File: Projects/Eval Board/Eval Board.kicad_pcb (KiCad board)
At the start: 4 copper layers, 46 x 27.3 mm, 37 parts, among them J1 LO, J2 Q OUT, J3 I Out, J4 Q OUT, J6 Conn_01x02, J7 Conn_01x04, J8 Conn_01x05, U1 LTC5584

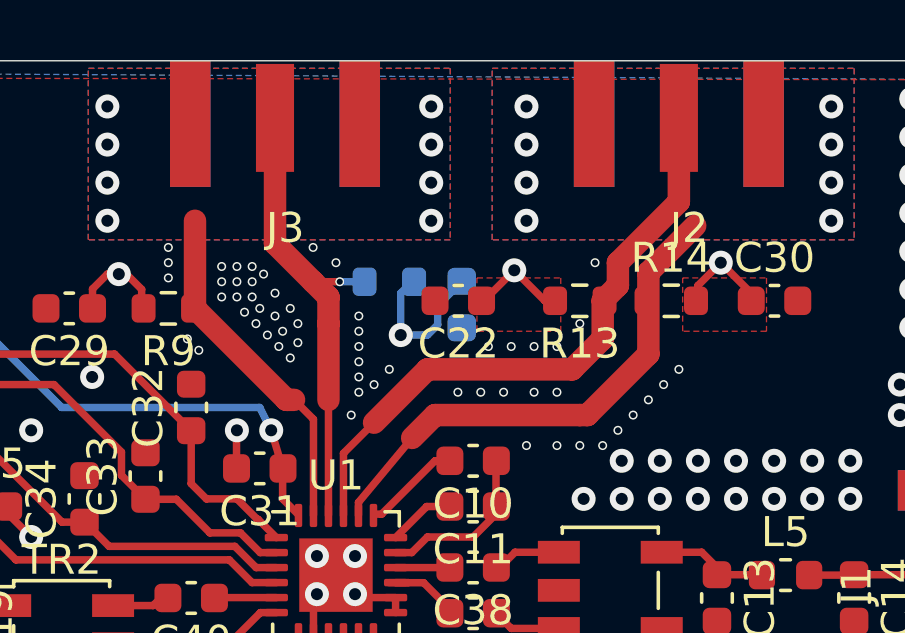
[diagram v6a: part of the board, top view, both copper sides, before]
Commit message: Widened the traces on the I+-/Q+- to be 1mm
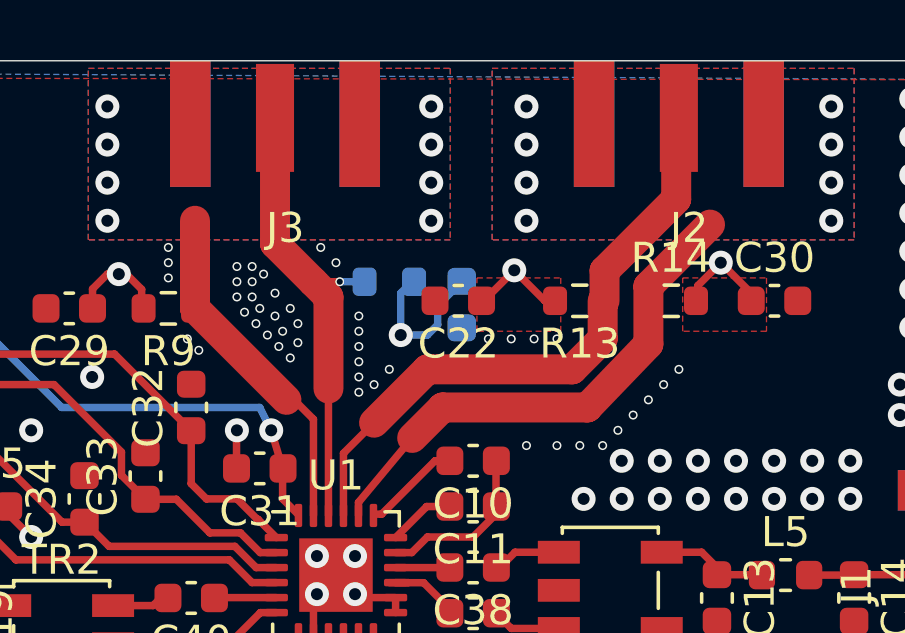
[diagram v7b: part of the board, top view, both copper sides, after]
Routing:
- net /Q+: track 21.0 -> 26.9 mm
- net GND: vias 199 -> 188
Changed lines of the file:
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@@
     (thickness 1.6)
     (drawings 8)
-    (tracks 407)
+    (tracks 396)
     (zones 0)
     (modules 37)
@@
   )
   (setup
-    (last_trace_width 0.75)
+    (last_trace_width 1)
     (user_trace_width 0.5)
     (user_trace_width 0.75)
@@
   (segment (start 194.83 83.554) (end 195.072 83.312) (width 0.25) (layer F.Cu) (net 4) (status 30))
   (segment (start 194.83 84.5375) (end 194.83 83.554) (width 0.25) (layer F.Cu) (net 4) (status 30))
-  (via (at 191.77 73.279) (size 0.3) (drill 0.2) (layers F.Cu B.Cu) (net 4))
-  (via (at 191.77 72.771) (size 0.3) (drill 0.2) (layers F.Cu B.Cu) (net 4))
-  (via (at 191.77 72.263) (size 0.3) (drill 0.2) (layers F.Cu B.Cu) (net 4))
   (via (at 192.278 72.263) (size 0.3) (drill 0.2) (layers F.Cu B.Cu) (net 4))
   (via (at 192.786 72.263) (size 0.3) (drill 0.2) (layers F.Cu B.Cu) (net 4))
@@
   (via (at 189.992 72.136) (size 0.3) (drill 0.2) (layers F.Cu B.Cu) (net 4))
   (via (at 189.992 71.628) (size 0.3) (drill 0.2) (layers F.Cu B.Cu) (net 4))
-  (via (at 199.644 76.454) (size 0.3) (drill 0.2) (layers F.Cu B.Cu) (net 4))
-  (via (at 200.406 76.454) (size 0.3) (drill 0.2) (layers F.Cu B.Cu) (net 4))
-  (via (at 201.168 76.454) (size 0.3) (drill 0.2) (layers F.Cu B.Cu) (net 4))
-  (via (at 202.184 76.454) (size 0.3) (drill 0.2) (layers F.Cu B.Cu) (net 4))
-  (via (at 202.946 76.454) (size 0.3) (drill 0.2) (layers F.Cu B.Cu) (net 4))
   (via (at 207.01 75.692) (size 0.3) (drill 0.2) (layers F.Cu B.Cu) (net 4))
   (via (at 206.502 76.2) (size 0.3) (drill 0.2) (layers F.Cu B.Cu) (net 4))
@@
   (via (at 202.946 78.232) (size 0.3) (drill 0.2) (layers F.Cu B.Cu) (net 4))
   (via (at 204.978 77.724) (size 0.3) (drill 0.2) (layers F.Cu B.Cu) (net 4))
-  (via (at 200.66 74.93) (size 0.3) (drill 0.2) (layers F.Cu B.Cu) (net 4))
-  (via (at 201.422 74.93) (size 0.3) (drill 0.2) (layers F.Cu B.Cu) (net 4))
-  (via (at 202.184 74.93) (size 0.3) (drill 0.2) (layers F.Cu B.Cu) (net 4))
-  (via (at 202.946 74.93) (size 0.3) (drill 0.2) (layers F.Cu B.Cu) (net 4))
-  (via (at 203.708 74.168) (size 0.3) (drill 0.2) (layers F.Cu B.Cu) (net 4))
-  (via (at 204.216 72.136) (size 0.3) (drill 0.2) (layers F.Cu B.Cu) (net 4))
+  (via (at 200.66 74.676) (size 0.3) (drill 0.2) (layers F.Cu B.Cu) (net 4))
+  (via (at 201.422 74.676) (size 0.3) (drill 0.2) (layers F.Cu B.Cu) (net 4))
+  (via (at 202.184 74.676) (size 0.3) (drill 0.2) (layers F.Cu B.Cu) (net 4))
+  (via (at 202.946 74.676) (size 0.3) (drill 0.2) (layers F.Cu B.Cu) (net 4))
   (via (at 196.85 76.2) (size 0.3) (drill 0.2) (layers F.Cu B.Cu) (net 4))
   (via (at 197.358 75.692) (size 0.3) (drill 0.2) (layers F.Cu B.Cu) (net 4))
-  (via (at 196.088 77.216) (size 0.3) (drill 0.2) (layers F.Cu B.Cu) (net 4))
   (via (at 193.802 74.422) (size 0.3) (drill 0.2) (layers F.Cu B.Cu) (net 4))
   (via (at 193.548 73.914) (size 0.3) (drill 0.2) (layers F.Cu B.Cu) (net 4))
   (via (at 195.58 72.136) (size 0.3) (drill 0.2) (layers F.Cu B.Cu) (net 4))
-  (via (at 194.818 71.628) (size 0.3) (drill 0.2) (layers F.Cu B.Cu) (net 4))
+  (via (at 195.072 71.628) (size 0.3) (drill 0.2) (layers F.Cu B.Cu) (net 4))
   (via (at 203.708 78.232) (size 0.3) (drill 0.2) (layers F.Cu B.Cu) (net 4))
   (via (at 204.47 78.232) (size 0.3) (drill 0.2) (layers F.Cu B.Cu) (net 4))
@@
   (segment (start 195.83 80.5625) (end 195.83 78.49) (width 0.25) (layer F.Cu) (net 18))
   (segment (start 195.83 78.49) (end 196.85 77.47) (width 0.25) (layer F.Cu) (net 18))
-  (segment (start 204.978 72.898) (end 204.978 72.136) (width 0.75) (layer F.Cu) (net 18))
   (segment (start 204.978 72.136) (end 207.01 70.104) (width 0.75) (layer F.Cu) (net 18))
   (segment (start 207.01 70.104) (end 207.01 67.056) (width 0.75) (layer F.Cu) (net 18))
-  (segment (start 196.85 77.47) (end 198.628 75.692) (width 0.75) (layer F.Cu) (net 18))
-  (segment (start 198.628 75.692) (end 203.454 75.692) (width 0.75) (layer F.Cu) (net 18))
-  (segment (start 203.454 75.692) (end 204.47 74.676) (width 0.75) (layer F.Cu) (net 18))
-  (segment (start 204.47 73.406) (end 204.978 72.898) (width 0.75) (layer F.Cu) (net 18))
-  (segment (start 204.47 74.676) (end 204.47 73.406) (width 0.75) (layer F.Cu) (net 18))
+  (segment (start 196.85 77.47) (end 198.628 75.692) (width 1) (layer F.Cu) (net 18))
+  (segment (start 198.628 75.692) (end 203.454 75.692) (width 1) (layer F.Cu) (net 18))
+  (segment (start 203.454 75.692) (end 204.47 74.676) (width 1) (layer F.Cu) (net 18))
+  (segment (start 204.47 74.676) (end 204.47 73.406) (width 1) (layer F.Cu) (net 18))
+  (segment (start 204.533 72.404224) (end 206.921612 70.015612) (width 1) (layer F.Cu) (net 18))
+  (segment (start 204.533 73.406) (end 204.533 72.404224) (width 1) (layer F.Cu) (net 18))
+  (segment (start 206.921612 70.015612) (end 206.921612 67.144388) (width 1) (layer F.Cu) (net 18))
+  (segment (start 206.921612 67.144388) (end 207.01 67.056) (width 1) (layer F.Cu) (net 18))
   (segment (start 195.33 80.5625) (end 195.33 76.712) (width 0.25) (layer F.Cu) (net 19))
-  (segment (start 193.548 71.501) (end 193.548 67.056) (width 0.75) (layer F.Cu) (net 19))
-  (segment (start 195.33 76.712) (end 195.33 74.172) (width 0.75) (layer F.Cu) (net 19))
-  (segment (start 195.33 74.172) (end 195.33 73.283) (width 0.75) (layer F.Cu) (net 19))
-  (segment (start 195.33 73.283) (end 194.818 72.771) (width 0.75) (layer F.Cu) (net 19))
-  (segment (start 194.818 72.771) (end 193.548 71.501) (width 0.75) (layer F.Cu) (net 19))
+  (segment (start 193.548 71.501) (end 193.548 67.056) (width 1) (layer F.Cu) (net 19))
+  (segment (start 194.818 72.771) (end 193.548 71.501) (width 1) (layer F.Cu) (net 19))
   (segment (start 195.072 72.771) (end 194.818 72.771) (width 0.25) (layer F.Cu) (net 19))
   (segment (start 195.707 72.771) (end 195.072 72.771) (width 0.25) (layer F.Cu) (net 19))
@@
   (segment (start 196.469 72.771) (end 196.596 72.898) (width 0.25) (layer B.Cu) (net 19))
   (segment (start 195.707 72.771) (end 196.469 72.771) (width 0.25) (layer B.Cu) (net 19))
+  (segment (start 195.33 76.712) (end 195.33 76.331) (width 0.25) (layer F.Cu) (net 19))
+  (segment (start 195.33 73.283) (end 194.818 72.771) (width 1) (layer F.Cu) (net 19))
+  (segment (start 195.33 76.331) (end 195.33 73.283) (width 1) (layer F.Cu) (net 19))
   (via (at 198.755 66.929) (size 0.8) (drill 0.4) (layers F.Cu B.Cu) (net 20))
   (via (at 198.755 68.199) (size 0.8) (drill 0.4) (layers F.Cu B.Cu) (net 20))
@@
   (segment (start 194.83 80.5625) (end 194.83 77.355) (width 0.25) (layer F.Cu) (net 20))
   (segment (start 194.83 77.355) (end 194.183 76.708) (width 0.25) (layer F.Cu) (net 20))
-  (segment (start 194.183 76.708) (end 193.929 76.708) (width 0.75) (layer F.Cu) (net 20))
-  (segment (start 193.929 76.708) (end 190.881 73.66) (width 0.75) (layer F.Cu) (net 20))
-  (segment (start 190.881 73.66) (end 190.881 70.739) (width 0.75) (layer F.Cu) (net 20))
+  (segment (start 193.929 76.708) (end 190.881 73.66) (width 1) (layer F.Cu) (net 20))
+  (segment (start 190.881 73.66) (end 190.881 70.739) (width 1) (layer F.Cu) (net 20))
   (via (at 212.09 66.929) (size 0.8) (drill 0.4) (layers F.Cu B.Cu) (net 21))
   (via (at 212.09 68.199) (size 0.8) (drill 0.4) (layers F.Cu B.Cu) (net 21))
@@
   (segment (start 196.33 80.126978) (end 198.12 77.978) (width 0.25) (layer F.Cu) (net 21))
   (segment (start 196.33 80.5625) (end 196.33 80.126978) (width 0.25) (layer F.Cu) (net 21))
-  (segment (start 198.12 77.978) (end 198.882 77.216) (width 0.75) (layer F.Cu) (net 21))
-  (segment (start 198.882 77.216) (end 203.708 77.216) (width 0.75) (layer F.Cu) (net 21))
-  (segment (start 203.708 77.216) (end 203.962 77.216) (width 0.75) (layer F.Cu) (net 21))
-  (segment (start 203.962 77.216) (end 205.994 75.184) (width 0.75) (layer F.Cu) (net 21))
-  (segment (start 205.994 75.184) (end 205.994 72.463516) (width 0.75) (layer F.Cu) (net 21))
-  (segment (start 205.994 72.463516) (end 207.554758 70.902758) (width 0.75) (layer F.Cu) (net 21))
+  (segment (start 205.994 72.920998) (end 208.048998 70.866) (width 1) (layer F.Cu) (net 21))
+  (segment (start 205.994 74.84907) (end 205.994 72.920998) (width 1) (layer F.Cu) (net 21))
+  (segment (start 203.962 76.962) (end 205.994 74.84907) (width 1) (layer F.Cu) (net 21))
+  (segment (start 199.136 76.962) (end 203.962 76.962) (width 1) (layer F.Cu) (net 21))
+  (segment (start 198.12 77.978) (end 199.136 76.962) (width 1) (layer F.Cu) (net 21))
   (segment (start 190.754 79.502) (end 190.754 77.724) (width 0.25) (layer F.Cu) (net 22) (status 20))
   (segment (start 191.262 80.01) (end 190.754 79.502) (width 0.25) (layer F.Cu) (net 22))
